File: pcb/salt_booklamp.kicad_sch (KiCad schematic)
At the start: 33 parts, among them J1 USB-C31-S-RA-CS1E-BK-T/R, P1 PIC-TC2050-IDC, U1 PIC16F15213T-I/MF, U2 BQ21040DBVR, U3 TPS61158DRVR

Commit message: ordered pca, wood, copper, batteries
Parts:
- removed R7: 0r0, Resistor_SMD:R_0402_1005Metric, symbol salt_booklamp:resistor
- R1, R3, R4, R5: Manufacturer Part Number RMCF0603FT10K0 -> RC0402JR-0710KL
- R10, R9: Manufacturer Part Number CR0603-FX-1201ELF -> ERA-2AEB512X
- R2: Manufacturer Part Number RMCF0603FT6R80 -> CRCW04026R80FKED
- R8: Manufacturer Part Number RC0603JR-070RL -> CRCW04020000Z0ED; now left out of the parts list
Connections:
- net +3.7_VBATT: now also U2.6 (VIN); no longer P1.4
- net +5V_USB: no longer P1.10
- net GND: now also S1.2; no longer P1.6
- net LED_CTRL: no longer P1.2
- net ~{CHARGING}: now also U2.5 (GND)
- net ~{SWITCH}: no longer P1.8
- net at R1.2: now also U2.4 (ISET)
- no-connect marks 15 -> 20
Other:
- moved on the sheet: U2

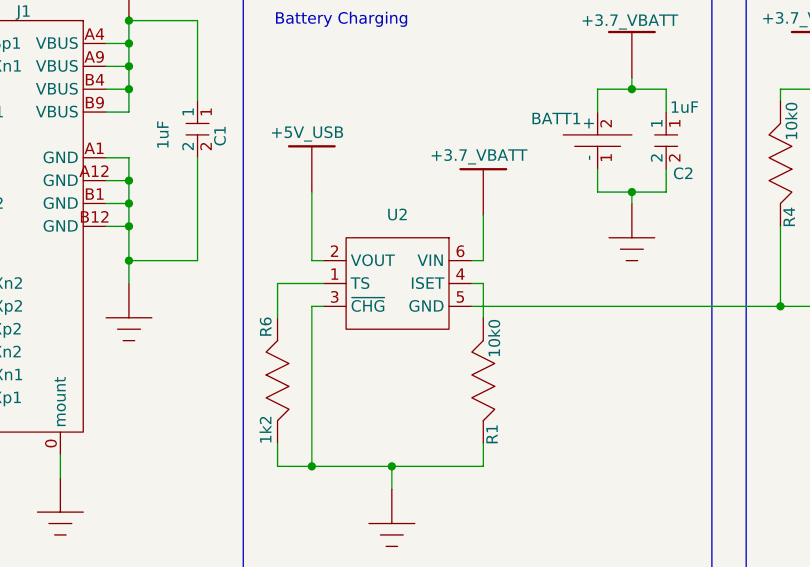
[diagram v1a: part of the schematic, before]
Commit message: build7 fixes - interposer for pcb error, new switch retainer, new mirror film, adhesive film to test
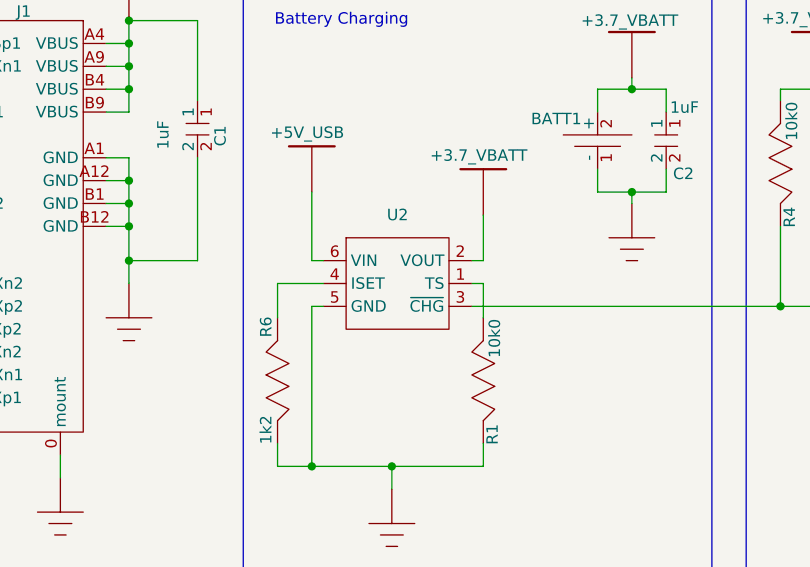
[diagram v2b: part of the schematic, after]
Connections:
- net +3.7_VBATT: now also U2.2 (VOUT); no longer U2.6 (VIN)
- net +5V_USB: now also U2.6 (VIN); no longer U2.2 (VOUT)
- net GND: now also U2.5 (GND); no longer U2.3 (~{CHG})
- net ~{CHARGING}: now also U2.3 (~{CHG}); no longer U2.5 (GND)
- net at R1.2: now also U2.1 (TS); no longer U2.4 (ISET)
- net at R6.1: now also U2.4 (ISET); no longer U2.1 (TS)
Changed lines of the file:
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@@
 	(wire
 		(pts
+			(xy 86.36 109.22) (xy 87.63 109.22)
+		)
+		(stroke
+			(width 0)
+			(type default)
+		)
+	)
+	(wire
+		(pts
 			(xy 252.73 119.38) (xy 252.73 146.05)
 		)
@@
 	(wire
 		(pts
-			(xy 86.36 109.22) (xy 87.63 109.22)
-		)
-		(stroke
-			(width 0)
-			(type default)
-		)
-	)
-	(wire
-		(pts
 			(xy 247.65 109.22) (xy 247.65 102.87)
 		)
@@
 	(wire
 		(pts
-			(xy 87.63 113.03) (xy 87.63 109.22)
+			(xy 87.63 109.22) (xy 87.63 113.03)
 		)
 		(stroke
@@
 	(symbol
 		(lib_id "salt_booklamp:batt_chg_ic_BQ21040DBVR")
-		(at 78.74 109.22 0)
-		(mirror y)
+		(at 77.47 109.22 0)
 		(unit 1)
 		(exclude_from_sim yes)
@@
 		)
 		(property "Value" "BQ21040DBVR"
-			(at 78.486 115.824 0)
+			(at 77.724 115.824 0)
 			(effects
 				(font
@@
 		)
 		(property "Footprint" "salt_booklamp_footprints:BQ21040DBVR"
-			(at 78.232 117.094 0)
+			(at 77.978 117.094 0)
 			(effects
 				(font
@@
 		)
 		(property "Datasheet" "${KIPRJMOD}/lib/Datasheets/bq21040.pdf"
-			(at 78.74 109.22 0)
+			(at 77.47 109.22 0)
 			(effects
 				(font
@@
 		)
 		(property "Description" "IC BATT CHG LI-ION 1CELL SOT23-6"
-			(at 78.74 109.22 0)
+			(at 77.47 109.22 0)
 			(effects
 				(font
@@
 		)
 		(property "Digikey" "https://www.digikey.com/en/products/detail/texas-instruments/BQ21040DBVR/6036340"
-			(at 78.74 109.22 0)
+			(at 77.47 109.22 0)
 			(effects
 				(font
@@
 		)
 		(property "Manufacturer Part Number" "BQ21040DBVR"
-			(at 78.486 115.824 0)
+			(at 77.724 115.824 0)
 			(effects
 				(font

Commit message: Current status: debugged and fixed 4 boards, need to finalize firmware and finish building these 4. All lamps from first build came unglued, need to revise design/assembly to fix this
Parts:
- TP_3.7V_BATT1, TP_5V_USB1, TP_GND1, TP_LED_CTRL1, TP_LED_DRV1, TP_~{CHARGING}1, TP_~{SWITCH}1: value ~ -> (none)
